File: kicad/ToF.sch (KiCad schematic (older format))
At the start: 7 parts, among them P7 ToF_Host, P8 ToF_Slave, U7 VL53L0X

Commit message: 回路を改良
受光部をフォトトランジスタに変更
測距センサをVL6180Xに変更
動作電圧を3Vに変更
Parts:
- removed R16, R17: 4.7k, Resistors_SMD:R_0201, symbol R_Small
- removed U7: VL53L0X, mouse:VL53L0X, symbol VL53L0X
- added U5: VL6180X, mouse:VL6180X, symbol VL6180X
- renumbered C17 to C11, C18 to C12
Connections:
- wire segments 31 -> 22
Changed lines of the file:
@@
 LIBS:ftdi
 LIBS:gennum
-LIBS:graphic
 LIBS:hc11
 LIBS:ir
 LIBS:Lattice
 LIBS:leds
-LIBS:logo
 LIBS:maxim
 LIBS:mechanical
@@
 LIBS:zetex
 LIBS:Zilog
+LIBS:graphic_symbols
+LIBS:infineon
+LIBS:intersil
+LIBS:LEM
+LIBS:logic_programmable
+LIBS:RFSolutions
 LIBS:KERISE-cache
 EELAYER 25 0
@@
 Comment4 ""
 $EndDescr
-$Comp
-L VL53L0X U7
-U 1 1 592B9F2C
-P 4800 3300
-F 0 "U7" H 4800 3450 60  0000 C CNN
-F 1 "VL53L0X" H 4800 3300 60  0000 C CNN
-F 2 "mouse:VL53L0X" H 4800 3300 60  0001 C CNN
-F 3 "" H 4800 3300 60  0000 C CNN
-	1    4800 3300
-	1    0    0    -1
-$EndComp
-Wire Wire Line
-	4200 3300 4200 3500
-Wire Wire Line
-	4200 3400 4300 3400
-Wire Wire Line
-	4200 3500 4300 3500
-Connection ~ 4200 3400
-Wire Wire Line
-	4200 3700 4200 4200
-Wire Wire Line
-	4200 4100 4300 4100
-Wire Wire Line
-	4200 4000 4300 4000
-Connection ~ 4200 4100
-Wire Wire Line
-	4200 3900 4300 3900
-Connection ~ 4200 4000
-Wire Wire Line
-	4200 3800 4300 3800
-Connection ~ 4200 3900
-Wire Wire Line
-	4200 3700 4300 3700
-Connection ~ 4200 3800
 Text HLabel 4300 2400 0    60   Input ~ 0
 SDA
 Text HLabel 4300 2500 0    60   Input ~ 0
 SCL
-Wire Wire Line
-	5300 3700 5800 3700
-Wire Wire Line
-	5300 3800 6100 3800
-Wire Wire Line
-	5400 3400 5300 3400
-$Comp
-L C_Small C18
+$Comp
+L C_Small C12
 U 1 1 592BA26F
 P 3900 3800
-F 0 "C18" H 3910 3870 50  0000 L CNN
+F 0 "C12" H 3910 3870 50  0000 L CNN
 F 1 "0.1u" H 3910 3720 50  0000 L CNN
 F 2 "Capacitors_SMD:C_0201" H 3900 3800 50  0001 C CNN
@@
 $EndComp
 $Comp
-L C_Small C17
+L C_Small C11
 U 1 1 592BA2BF
 P 3600 3800
-F 0 "C17" H 3610 3870 50  0000 L CNN
+F 0 "C11" H 3610 3870 50  0000 L CNN
 F 1 "4.7u" H 3610 3720 50  0000 L CNN
 F 2 "Capacitors_SMD:C_0402" H 3600 3800 50  0001 C CNN
@@
 	1    0    0    -1
 $EndComp
-Wire Wire Line
-	3600 3300 3600 3700
-Wire Wire Line
-	3900 3700 3900 3300
-Wire Wire Line
-	3900 3900 3900 4200
-Wire Wire Line
-	3600 4200 3600 3900
 Text Label 3600 3300 1    60   ~ 0
 s_3.3V
@@
 Text Label 4200 4200 3    60   ~ 0
 s_GND
-Text Label 5400 3300 1    60   ~ 0
-s_3.3V
-Wire Wire Line
-	5400 3300 5400 3400
 $Comp
 L CONN_01X04 P7
@@
 $EndComp
 $Comp
-L GND #PWR054
+L GND #PWR052
 U 1 1 592ABB63
 P 4300 2700
-F 0 "#PWR054" H 4300 2450 50  0001 C CNN
+F 0 "#PWR052" H 4300 2450 50  0001 C CNN
 F 1 "GND" H 4300 2550 50  0000 C CNN
 F 2 "" H 4300 2700 50  0000 C CNN
@@
 	1    0    0    -1
 $EndComp
-Wire Wire Line
-	4300 2700 4300 2600
-Wire Wire Line
-	4300 2600 4400 2600
-$Comp
-L +3.3V #PWR055
+$Comp
+L +3.3V #PWR053
 U 1 1 592ABB9F
 P 4300 2200
-F 0 "#PWR055" H 4300 2050 50  0001 C CNN
+F 0 "#PWR053" H 4300 2050 50  0001 C CNN
 F 1 "+3.3V" H 4300 2340 50  0000 C CNN
 F 2 "" H 4300 2200 50  0000 C CNN
@@
 	1    0    0    -1
 $EndComp
-Wire Wire Line
-	4300 2200 4300 2300
-Wire Wire Line
-	4300 2300 4400 2300
 Text Label 5300 2300 0    60   ~ 0
 s_3.3V
@@
 Text Label 5300 2400 0    60   ~ 0
 s_SDA
-Wire Wire Line
-	5300 2400 5200 2400
-Wire Wire Line
-	5200 2300 5300 2300
-Wire Wire Line
-	5300 2500 5200 2500
-Wire Wire Line
-	5200 2600 5300 2600
-Text Label 5400 3800 0    60   ~ 0
+Text Label 5300 3800 0    60   ~ 0
 s_SCL
-Text Label 5400 3700 0    60   ~ 0
+Text Label 5300 3700 0    60   ~ 0
 s_SDA
-NoConn ~ 5300 3500
-Wire Wire Line
-	4400 2400 4300 2400
-Wire Wire Line
-	4300 2500 4400 2500
 Text Notes 3450 1950 0    100  ~ 0
 ToF
 $Comp
-L PWR_FLAG #FLG056
+L PWR_FLAG #FLG054
 U 1 1 592CE2A7
 P 5300 2300
-F 0 "#FLG056" H 5300 2395 50  0001 C CNN
+F 0 "#FLG054" H 5300 2395 50  0001 C CNN
 F 1 "PWR_FLAG" H 5300 2480 50  0000 C CNN
 F 2 "" H 5300 2300 50  0000 C CNN
@@
 $EndComp
 $Comp
-L PWR_FLAG #FLG057
+L PWR_FLAG #FLG055
 U 1 1 592CE368
 P 5300 2600
-F 0 "#FLG057" H 5300 2695 50  0001 C CNN
+F 0 "#FLG055" H 5300 2695 50  0001 C CNN
 F 1 "PWR_FLAG" H 5300 2780 50  0000 C CNN
 F 2 "" H 5300 2600 50  0000 C CNN
@@
 $EndComp
 $Comp
-L R_Small R16
-U 1 1 5932174C
-P 5800 3500
-F 0 "R16" H 5830 3520 50  0000 L CNN
-F 1 "4.7k" H 5830 3460 50  0000 L CNN
-F 2 "Resistors_SMD:R_0201" H 5800 3500 50  0001 C CNN
-F 3 "" H 5800 3500 50  0000 C CNN
-	1    5800 3500
-	1    0    0    -1
-$EndComp
-$Comp
-L R_Small R17
-U 1 1 593217CA
-P 6100 3500
-F 0 "R17" H 6130 3520 50  0000 L CNN
-F 1 "4.7k" H 6130 3460 50  0000 L CNN
-F 2 "Resistors_SMD:R_0201" H 6100 3500 50  0001 C CNN
-F 3 "" H 6100 3500 50  0000 C CNN
-	1    6100 3500
-	1    0    0    -1
-$EndComp
-Wire Wire Line
-	6100 3800 6100 3600
-Wire Wire Line
-	5800 3700 5800 3600
-Text Label 5800 3300 1    60   ~ 0
-s_3.3V
-Wire Wire Line
-	5800 3300 5800 3400
-Text Label 6100 3300 1    60   ~ 0
-s_3.3V
-Wire Wire Line
-	6100 3300 6100 3400
+L VL6180X U5
+U 1 1 5A4CAC8D
+P 4800 3300
+F 0 "U5" H 4800 3450 60  0000 C CNN
+F 1 "VL6180X" H 4800 3300 60  0000 C CNN
+F 2 "mouse:VL6180X" H 4800 3300 60  0001 C CNN
+F 3 "" H 4800 3300 60  0000 C CNN
+	1    4800 3300
+	1    0    0    -1
+$EndComp
+Text Label 5400 3300 1    60   ~ 0
+s_3.3V
+Wire Wire Line
+	5400 3300 5400 3400
+Wire Wire Line
+	4200 4000 4200 4200
+Wire Wire Line
+	4300 2500 4400 2500
+Wire Wire Line
+	4400 2400 4300 2400
+Wire Wire Line
+	5200 2600 5300 2600
+Wire Wire Line
+	5300 2500 5200 2500
+Wire Wire Line
+	5200 2300 5300 2300
+Wire Wire Line
+	5300 2400 5200 2400
+Wire Wire Line
+	4300 2300 4400 2300
+Wire Wire Line
+	4300 2200 4300 2300
+Wire Wire Line
+	4300 2600 4400 2600
+Wire Wire Line
+	4300 2700 4300 2600
+Wire Wire Line
+	3600 4200 3600 3900
+Wire Wire Line
+	3900 3900 3900 4200
+Wire Wire Line
+	3900 3700 3900 3300
+Wire Wire Line
+	3600 3300 3600 3700
+Connection ~ 4200 4100
+Wire Wire Line
+	4200 4000 4300 4000
+Wire Wire Line
+	4200 4100 4300 4100
+Connection ~ 4200 3400
+Wire Wire Line
+	4200 3500 4300 3500
+Wire Wire Line
+	4200 3400 4300 3400
+Wire Wire Line
+	4200 3300 4200 3500
+NoConn ~ 5300 3500
+Wire Wire Line
+	5400 3400 5300 3400
 $EndSCHEMATC

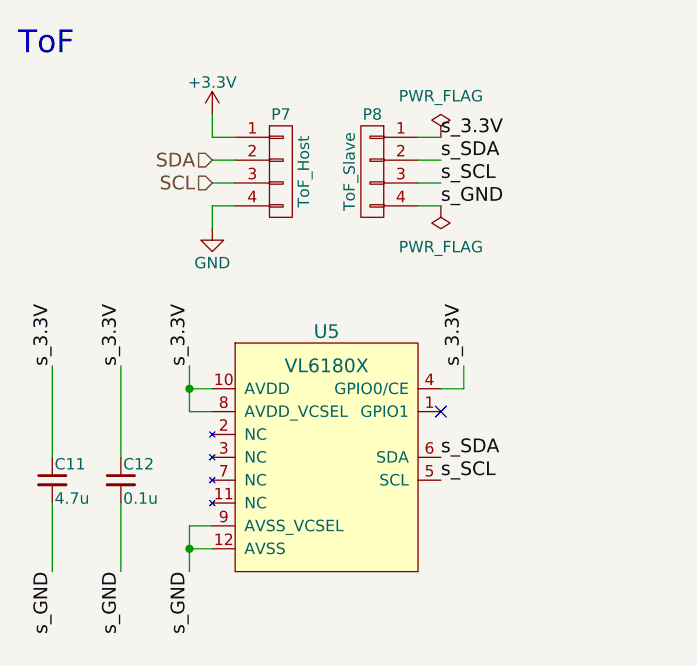
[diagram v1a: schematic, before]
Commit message: 部品を配置
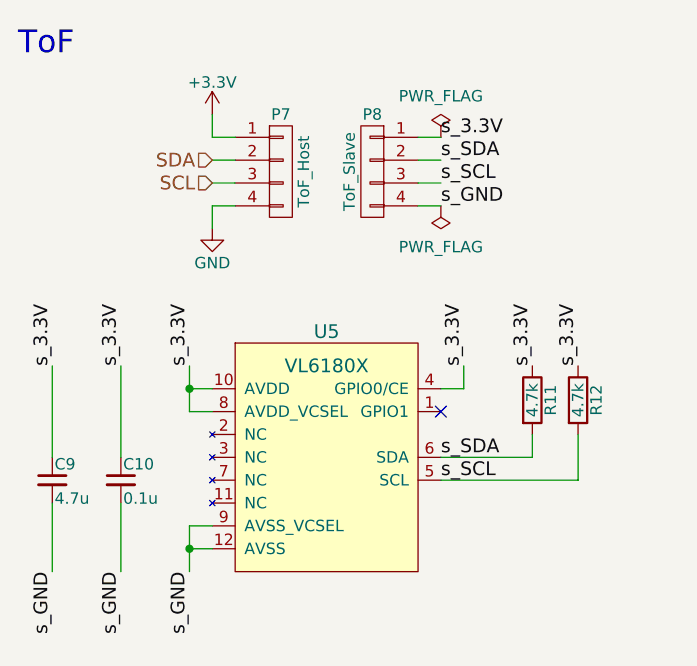
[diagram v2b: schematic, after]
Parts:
- added R11, R12: 4.7k, Resistors_SMD:R_0201_NoSilk, symbol R
- C10: renamed from C12; footprint Capacitors_SMD:C_0201 -> Capacitors_SMD:C_0201_NoSilk
- C9: renamed from C11; footprint Capacitors_SMD:C_0402 -> Capacitors_SMD:C_0402_NoSilk
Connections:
- net s_3.3V: now also R11.1, R12.1
- net s_SCL: now also R12.2
- net s_SDA: now also R11.2
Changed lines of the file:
@@
 $Descr A4 11693 8268
 encoding utf-8
-Sheet 9 15
+Sheet 9 16
 Title ""
 Date ""
@@
 SCL
 $Comp
-L C_Small C12
+L C_Small C10
 U 1 1 592BA26F
 P 3900 3800
-F 0 "C12" H 3910 3870 50  0000 L CNN
+F 0 "C10" H 3910 3870 50  0000 L CNN
 F 1 "0.1u" H 3910 3720 50  0000 L CNN
-F 2 "Capacitors_SMD:C_0201" H 3900 3800 50  0001 C CNN
+F 2 "Capacitors_SMD:C_0201_NoSilk" H 3900 3800 50  0001 C CNN
 F 3 "" H 3900 3800 50  0000 C CNN
 	1    3900 3800
@@
 $EndComp
 $Comp
-L C_Small C11
+L C_Small C9
 U 1 1 592BA2BF
 P 3600 3800
-F 0 "C11" H 3610 3870 50  0000 L CNN
+F 0 "C9" H 3610 3870 50  0000 L CNN
 F 1 "4.7u" H 3610 3720 50  0000 L CNN
-F 2 "Capacitors_SMD:C_0402" H 3600 3800 50  0001 C CNN
+F 2 "Capacitors_SMD:C_0402_NoSilk" H 3600 3800 50  0001 C CNN
 F 3 "" H 3600 3800 50  0000 C CNN
 	1    3600 3800
@@
 $EndComp
 $Comp
-L GND #PWR052
+L GND #PWR050
 U 1 1 592ABB63
 P 4300 2700
-F 0 "#PWR052" H 4300 2450 50  0001 C CNN
+F 0 "#PWR050" H 4300 2450 50  0001 C CNN
 F 1 "GND" H 4300 2550 50  0000 C CNN
 F 2 "" H 4300 2700 50  0000 C CNN
@@
 $EndComp
 $Comp
-L +3.3V #PWR053
+L +3.3V #PWR051
 U 1 1 592ABB9F
 P 4300 2200
-F 0 "#PWR053" H 4300 2050 50  0001 C CNN
+F 0 "#PWR051" H 4300 2050 50  0001 C CNN
 F 1 "+3.3V" H 4300 2340 50  0000 C CNN
 F 2 "" H 4300 2200 50  0000 C CNN
@@
 ToF
 $Comp
-L PWR_FLAG #FLG054
+L PWR_FLAG #FLG052
 U 1 1 592CE2A7
 P 5300 2300
-F 0 "#FLG054" H 5300 2395 50  0001 C CNN
+F 0 "#FLG052" H 5300 2395 50  0001 C CNN
 F 1 "PWR_FLAG" H 5300 2480 50  0000 C CNN
 F 2 "" H 5300 2300 50  0000 C CNN
@@
 $EndComp
 $Comp
-L PWR_FLAG #FLG055
+L PWR_FLAG #FLG053
 U 1 1 592CE368
 P 5300 2600
-F 0 "#FLG055" H 5300 2695 50  0001 C CNN
+F 0 "#FLG053" H 5300 2695 50  0001 C CNN
 F 1 "PWR_FLAG" H 5300 2780 50  0000 C CNN
 F 2 "" H 5300 2600 50  0000 C CNN
@@
 Wire Wire Line
 	5400 3400 5300 3400
+$Comp
+L R R11
+U 1 1 5AB6394F
+P 5700 3450
+F 0 "R11" V 5780 3450 50  0000 C CNN
+F 1 "4.7k" V 5700 3450 50  0000 C CNN
+F 2 "Resistors_SMD:R_0201_NoSilk" V 5630 3450 50  0001 C CNN
+F 3 "" H 5700 3450 50  0001 C CNN
+	1    5700 3450
+	1    0    0    -1
+$EndComp
+$Comp
+L R R12
+U 1 1 5AB639A9
+P 5900 3450
+F 0 "R12" V 5980 3450 50  0000 C CNN
+F 1 "4.7k" V 5900 3450 50  0000 C CNN
+F 2 "Resistors_SMD:R_0201_NoSilk" V 5830 3450 50  0001 C CNN
+F 3 "" H 5900 3450 50  0001 C CNN
+	1    5900 3450
+	1    0    0    -1
+$EndComp
+Wire Wire Line
+	5900 3600 5900 3800
+Wire Wire Line
+	5900 3800 5300 3800
+Wire Wire Line
+	5300 3700 5700 3700
+Wire Wire Line
+	5700 3700 5700 3600
+Text Label 5700 3300 1    60   ~ 0
+s_3.3V
+Text Label 5900 3300 1    60   ~ 0
+s_3.3V
 $EndSCHEMATC
